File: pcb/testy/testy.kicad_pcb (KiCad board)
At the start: 2 copper layers, 144.9 x 102 mm, 83 parts, among them J1 Conn_01x02, J2 Conn_01x02, SW0:0 SW_Push, SW0:1 SW_Push, SW0:2 SW_Push, SW0:3 SW_Push, SW0:4 SW_Push, SW0:5 SW_Push, SW1:0 SW_Push, SW1:1 SW_Push, SW1:2 SW_Push, SW1:3 SW_Push, SW1:4 SW_Push, SW1:5 SW_Push, SW2:0 SW_Push, SW2:1 SW_Push, SW2:2 SW_Push, SW2:3 SW_Push, SW2:4 SW_Push, SW2:5 SW_Push, SW3:0 SW_Push, SW3:1 SW_Push, SW3:2 SW_Push, SW3:3 SW_Push, SW3:4 SW_Push, SW3:5 SW_Push, SW3:6 SW_Push, SW4:0 SW_Push, SW4:1 SW_Push, SW4:2 SW_Push, SW4:3 SW_Push, SW4:4 SW_Push, SW4:5 SW_Push, SW4:6 SW_Push, U1 ProMicro

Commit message: feat: move to new 5 col version
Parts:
- removed D0:5, D1:5, D2:5, D3:6, D4:0, D4:6: 1N4148, Diode_THT:D_DO-35_SOD27_P7.62mm_Horizontal
- removed the Drill at (167.7, 68.4)
- removed J1, J2: Conn_01x02, footprints:edge-connector
- removed LED0: LED, footprints:LED_D3.0mm
- removed LED1, LED2: LED, LED_THT:LED_D3.0mm
- removed SW0:5, SW1:5, SW2:5, SW3:6, SW4:0, SW4:6: SW_Push, footprints:kailh-socket-and-choc-solder-reversible
- D3:0, D4:1: moved to B.Cu
- moved Drill 70.5 mm to (166.0, 69.2)
- moved TRRS1 32.9 mm to (185.8, 86.9)
- moved U1 24.5 mm to (177.4, 64.1)
- moved Drill 19.7 mm to (143.0, 124.1)
- moved SW-reset1 16.9 mm to (177.9, 99.4)
- moved SW-reset2 16.9 mm to (177.9, 97.8)
- moved SW-reset3 16.9 mm to (177.9, 97.8)
- moved D3:0 10.5 mm to (90.3, 115.4), turned to 270 degrees
- moved D4:1 9.38 mm to (109.3, 128.1)
- moved D4:5 8.42 mm to (168.8, 128.1)
- moved SW4:5 8.42 mm to (177.2, 135.7)
- moved D4:3 7.47 mm to (130.8, 128.1)
- moved SW4:1 7.47 mm to (101.2, 135.8), turned to 180 degrees
- moved SW4:2 7.47 mm to (120.2, 135.8)
- moved SW4:3 7.47 mm to (139.2, 135.8)
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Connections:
- net Net-(U1-Pad13) renamed LED
- net Net-(U1-Pad17) renamed SDA
- U1 pad 12: LED2 -> Net-(U1-Pad12)
- U1 pad 18: LED0 -> SCL
- U1 pad 24: LED1 -> Net-(U1-Pad24)
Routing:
- net Row4: track 203.5 -> 38.0 mm, vias 2 -> 0
- net Col5: track 177.1 -> 30.0 mm, vias 7 -> 1
- net Row3: track 104.5 -> 14.7 mm
- net Row2: track 86.2 -> 18.1 mm
- net Row1: track 86.0 -> 17.9 mm
- net Row0: track 86.9 -> 19.1 mm
- net Col6: track 45.8 -> 0.00 mm, vias 1 -> 0
- net Col0: track 121.8 -> 79.6 mm
- net Net-(D2:5-Pad2): track 29.1 -> 0.00 mm, vias 1 -> 0
- net Net-(D0:5-Pad2): track 29.1 -> 0.00 mm, vias 1 -> 0
- net Net-(D4:6-Pad2): track 29.1 -> 0.00 mm, vias 1 -> 0
- net Net-(D4:0-Pad2): track 29.1 -> 0.00 mm, vias 1 -> 0
- net Net-(D3:6-Pad2): track 29.1 -> 0.00 mm, vias 1 -> 0
- net Net-(D1:5-Pad2): track 29.1 -> 0.00 mm, vias 1 -> 0
- net Col2: track 93.2 -> 64.5 mm
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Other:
- board size 144.9 x 102 mm -> 114.5 x 101.4 mm
- board text added: "TODO add WSxxxx LED here?"
- board text added: "TODO add cuts around promicro, etc"
- board text added: "TODO align SW4:4 properly"
- board text removed: "<-- add mount for USB-C breakout board Only need mechanical mounting as electrically it'll be a flying lead"
- board text removed: "<-- add snapoff piece that can be soldered in as a thumb rest when SW4:5 is moved"
- board text removed: "<-- are edge fingers ok, or should we do through holes an mount the extra piece slight higher? Wire pads up in schematic"
- board text removed: "<-- look at moving ProMicro lower so USB-C breakout and protrude and protect the flying lead for the PM, but still be inside the rectangle footprint"
- board text removed: "TODO add resistors for LEDs"

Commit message: feat: lots done, still need more LEDs, the I2C resistors and finish the traces
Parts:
- added JP1: L_GND, footprints:Jumper, F.Cu at (181.5, 82.0)
- added JP2: L_VCC, footprints:Jumper, F.Cu at (179.0, 82.0)
- added JP3: L_SCL, footprints:Jumper, F.Cu at (176.4, 82.0)
- added JP4: L_SDA, footprints:Jumper, F.Cu at (173.9, 82.0)
- added JP5: R_SDA, footprints:Jumper, B.Cu at (173.9, 82.0)
- added JP6: R_SCL, footprints:Jumper, B.Cu at (176.4, 82.0)
- added JP7: R_VCC, footprints:Jumper, B.Cu at (179.0, 82.0)
- added JP8: R_GND, footprints:Jumper, B.Cu at (181.5, 82.0)
- added LED1: SK6812mini, footprints:ws2812-single, F.Cu at (181.4, 102.2)
- added P1: OLED, footprints:oled_header_helix, B.Cu at (181.5, 84.9)
- added P2: iCSP, footprints:PinHeader_1x06_P2.54mm_Vertical, F.Cu at (179.3, 65.2)
- added REF**: switchplate-brace, footprints:switchplate-brace, F.Cu at (185.5, 135.0)
- added REF**: switchplate-brace, footprints:switchplate-brace, F.Cu at (73.9, 85.0)
- added REF**: switchplate-brace, footprints:switchplate-brace, F.Cu at (73.8, 122.9)
- added REF**: switchplate-brace, footprints:switchplate-brace, F.Cu at (93.1, 135.0)
- added REF**: switchplate-brace, footprints:switchplate-brace, F.Cu at (126.5, 121.4)
- added REF**: switchplate-brace, footprints:switchplate-brace, F.Cu at (185.5, 115.6)
- added REF**: switchplate-brace, footprints:switchplate-brace, F.Cu at (163.8, 88.2)
- added REF**: switchplate-brace, footprints:switchplate-brace, F.Cu at (165.2, 50.6)
- added REF**: switchplate-brace, footprints:switchplate-brace, F.Cu at (135.1, 46.3)
- added REF**: switchplate-brace, footprints:switchplate-brace, F.Cu at (107.3, 46.2)
- added REF**: switchplate-brace, footprints:switchplate-brace, F.Cu at (74.9, 54.5)
- moved SW-reset1 106.1 mm to (83.8, 50.4), turned to 180 degrees
- moved SW-reset2 104.7 mm to (83.8, 51.9), turned to 270 degrees
- moved SW-reset3 104.7 mm to (83.8, 51.9), turned to 90 degrees
- moved Drill 23.1 mm to (154.3, 49.3)
- moved Drill 8.71 mm to (86.6, 113.6)
- moved Drill 7.17 mm to (89.1, 75.5)
- moved Drill 6.67 mm to (111.9, 122.9)
- moved TRRS1 5.48 mm to (186.8, 92.3)
- moved Drill 2.86 mm to (169.2, 105.5)
- moved Drill 1.52 mm to (142.2, 122.9)
- moved Drill 1.48 mm to (131.2, 66.1)
- moved Drill 1.46 mm to (131.2, 104.1)
- moved PM1 0.24 mm to (177.7, 64.1)
- moved D4:5 0.05 mm to (168.8, 128.1)
- moved SW4:4 0.05 mm to (158.2, 135.7)
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- renumbered U1 to PM1
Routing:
- net GND: track 0.00 -> 91.5 mm, vias 0 -> 2
- net Row3: track 14.7 -> 87.7 mm
- net LED: track 0.00 -> 71.8 mm, vias 0 -> 3
- net VCC: track 0.00 -> 65.0 mm, vias 0 -> 3
- net Col4: track 65.6 -> 125.1 mm, vias 1 -> 4
- net Row1: track 17.9 -> 71.8 mm
- net Row2: track 18.1 -> 71.8 mm
- net Row0: track 19.1 -> 72.4 mm
- net Col2: track 64.5 -> 113.1 mm, vias 1 -> 4
- net SDA: track 0.00 -> 27.0 mm, vias 0 -> 2
- net Col6: track 0.00 -> 24.3 mm
- net SCL: track 0.00 -> 22.3 mm, vias 0 -> 2
- net Row4: track 38.0 -> 59.8 mm
- net Col1: track 101.7 -> 121.5 mm, vias 4 -> 5
- net Col5: track 30.0 -> 48.7 mm
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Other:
- outline, holes or cut-outs redrawn
- board text added: "TODO add WSxxxx LED solder on points with jumpers to bypass"
- board text added: "v1.0"
- board text removed: "TODO add OLED headers. Copy layout of Helix"
- board text removed: "TODO add WSxxxx LED here?"
- board text removed: "TODO add cuts around promicro, etc"
- board text removed: "TODO align SW4:4 properly"

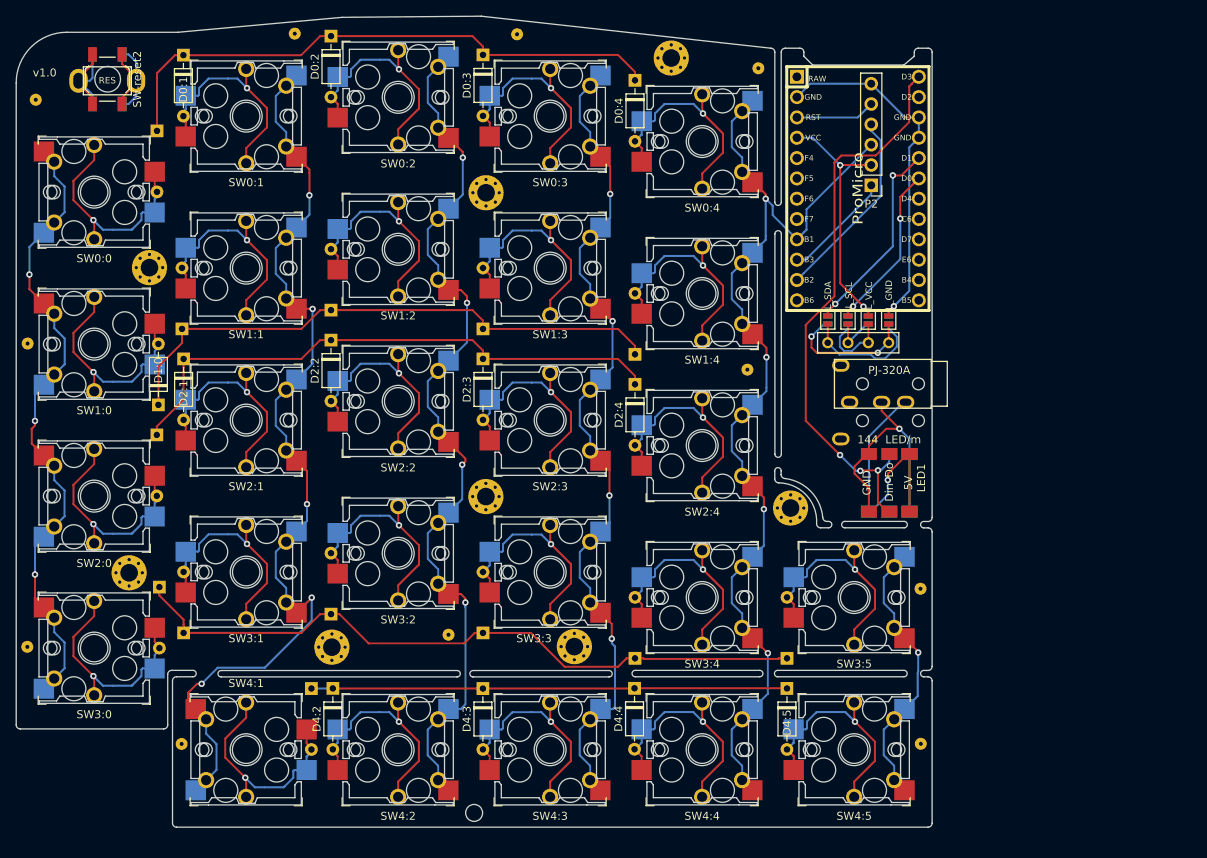
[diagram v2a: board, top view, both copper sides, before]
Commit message: feat: fully wired but stuff one side of the oled panels
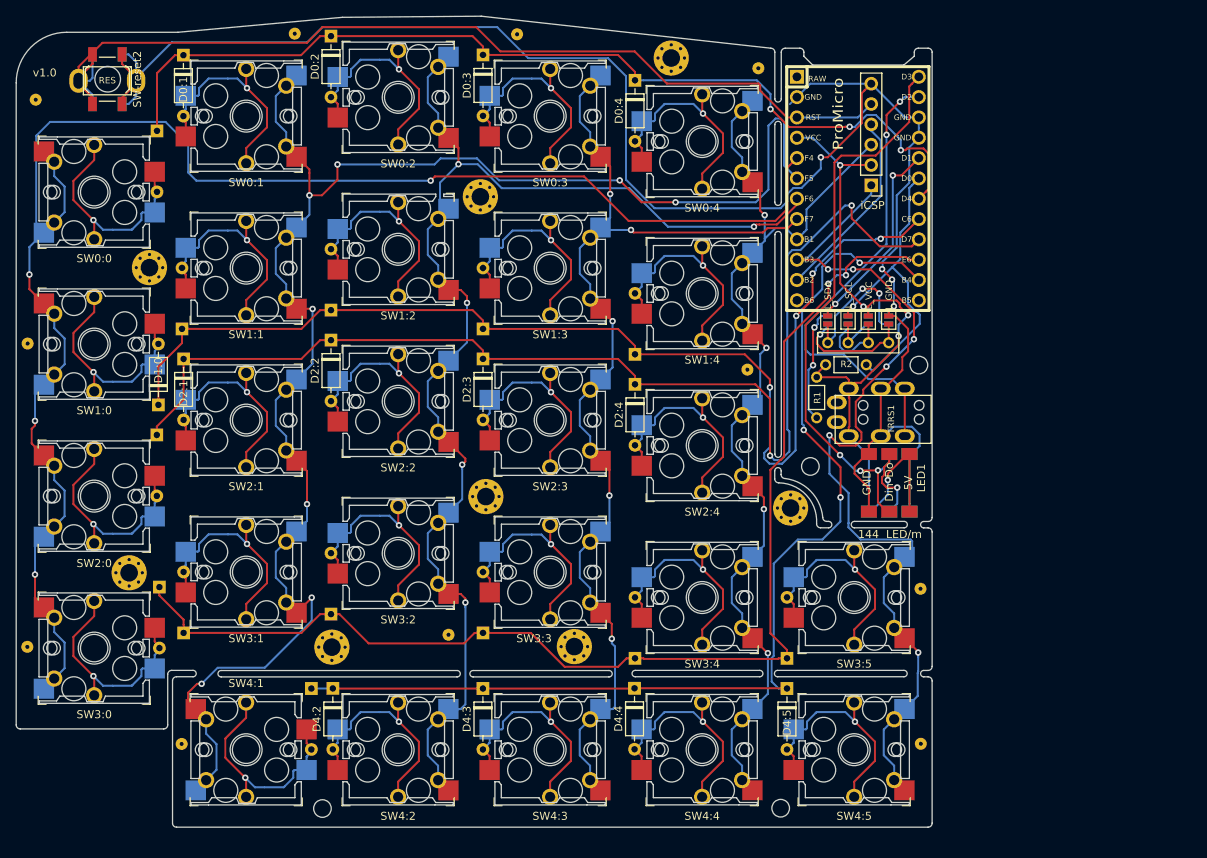
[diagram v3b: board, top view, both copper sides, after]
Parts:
- added HOLE_M2: VAL**, footprints:HOLE_M2, F.Cu at (185.3, 87.7)
- added HOLE_M2: VAL**, footprints:HOLE_M2, F.Cu at (171.7, 100.3)
- added HOLE_M2: VAL**, footprints:HOLE_M2, F.Cu at (110.7, 143.1)
- added HOLE_M2: VAL**, footprints:HOLE_M2, F.Cu at (168.0, 143.1)
- added R1: 4k7, footprints:resistor, F.Cu at (172.5, 91.7)
- added R2: 4k7, footprints:resistor, F.Cu at (176.2, 87.6)
- TRRS1: footprint footprints:TRRS-PJ-320A-dual -> footprints:TRRS-helix
- moved TRRS1 2.14 mm to (186.8, 94.5)
- moved Drill 0.87 mm to (130.5, 66.6)
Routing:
- net GND: track 91.5 -> 232.2 mm, vias 2 -> 4
- net Col0: track 79.6 -> 201.8 mm, vias 3 -> 4
- net Reset: track 26.1 -> 124.8 mm
- net Col1: track 121.5 -> 203.1 mm, vias 5 -> 8
- net Row4: track 59.8 -> 136.4 mm, vias 0 -> 3
- net Row2: track 71.8 -> 146.7 mm, vias 0 -> 2
- net Row1: track 71.8 -> 144.3 mm, vias 0 -> 4
- net Col5: track 48.7 -> 113.7 mm, vias 1 -> 6
- net Row3: track 87.7 -> 151.8 mm, vias 0 -> 2
- net data: track 0.00 -> 58.8 mm, vias 0 -> 2
- net Row0: track 72.4 -> 122.4 mm, vias 0 -> 3
- net Col2: track 113.1 -> 160.9 mm, vias 4 -> 5
- net VCC: track 65.0 -> 92.8 mm, vias 3 -> 5
- net Col3: track 105.8 -> 131.3 mm, vias 4 -> 5
- net SCL: track 22.3 -> 40.3 mm, vias 2 -> 1
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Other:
- outline, holes or cut-outs redrawn
- board text added: "FIXME the oled jumpers are oriented incorrectly, they should be a mirror?"
- board text added: "TODO add fill in thingy"

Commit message: feat: fill in zones, add instructions, correct OLED jumpers on right(bottom), still need to finalise LED wiring
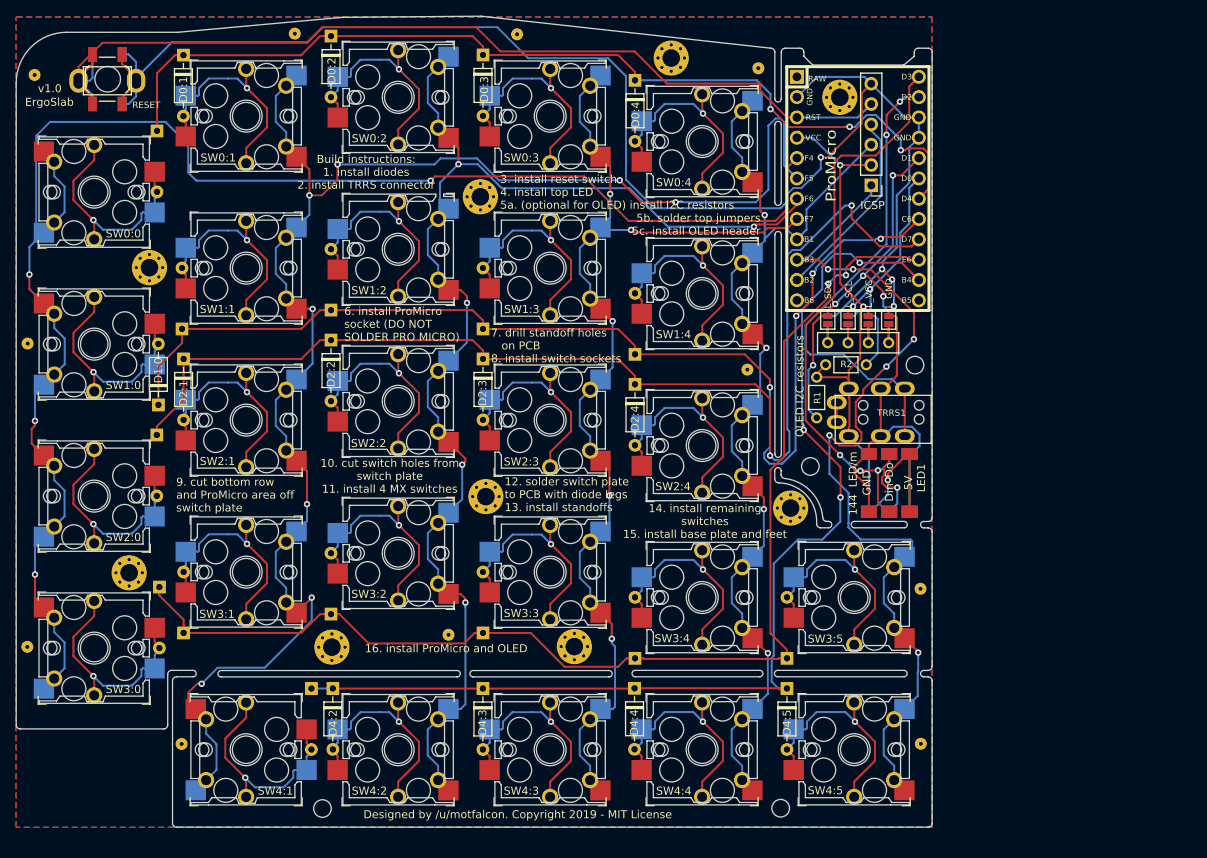
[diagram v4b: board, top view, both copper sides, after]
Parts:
- added Drill: MountingHole_2.2mm_M2_Pad_Via, MountingHole:MountingHole_2.2mm_M2_Pad_Via, F.Cu at (175.4, 54.2)
- P2: value iCSP -> ICSP
- moved JP8 7.61 mm to (173.9, 82.0)
- moved JP5 7.61 mm to (181.5, 82.0)
- moved REF** 3.10 mm to (74.8, 51.4)
- moved JP6 2.53 mm to (179.0, 82.0)
- moved JP7 2.53 mm to (176.4, 82.0)
- moved HOLE_M2 0.49 mm to (184.8, 87.7)
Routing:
- net Net-(JP4-Pad2): track 18.0 -> 4.71 mm, vias 2 -> 0
- net Net-(JP1-Pad2): track 15.8 -> 4.68 mm, vias 1 -> 0
- net SCL: track 40.3 -> 32.0 mm, vias 1 -> 2
- net VCC: track 92.8 -> 85.1 mm, vias 5 -> 3
- net GND: track 232.2 -> 238.3 mm
- net Net-(JP2-Pad2): track 9.82 -> 4.69 mm
- net SDA: track 41.6 -> 46.4 mm, vias 4 -> 5
- net Net-(TRRS1-Pad1): track 0.00 -> 2.45 mm
- net Net-(JP3-Pad2): track 5.85 -> 4.70 mm
- added copper zone on B.Cu, net (none)
- added copper zone on F.Cu, net (none)
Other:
- board text added: "10. cut switch holes from switch plate 11. install 4 MX switches"
- board text added: "12. solder switch plate to PCB with diode legs 13. install standoffs"
- board text added: "14. install remaining switches 15. install base plate and feet"
- board text added: "16. install ProMicro and OLED"
- board text added: "3. install reset switch 4. install top LED 5a. (optional for OLED) install I2C resistors"
- board text added: "5b. solder top jumpers 5c. install OLED header"
- board text added: "6. install ProMicro socket (DO NOT SOLDER PRO MICRO)"
- board text added: "7. drill standoff holes on PCB 8. install switch sockets"
- board text added: "9. cut bottom row and ProMicro area off switch plate"
- board text added: "Build instructions: 1. install diodes 2. install TRRS connector"
- board text added: "Designed by /u/motfalcon. Copyright 2019 - MIT License"
- board text added: "ErgoSlab"
- board text added: "OLED I2C resistors"
- board text removed: "FIXME the oled jumpers are oriented incorrectly, they should be a mirror?"
- board text removed: "TODO add fill in thingy"
